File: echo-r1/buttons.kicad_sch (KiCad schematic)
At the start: 14 parts, among them SW1 DPAD↑, SW10 X, SW11 Y, SW12 START, SW13 SELECT, SW14 HOLD, SW2 DPAD↓, SW3 DPAD←, SW4 DPAD→, SW5 A, SW6 B, SW7 VOL+, SW8 VOL-, SW9 POWER

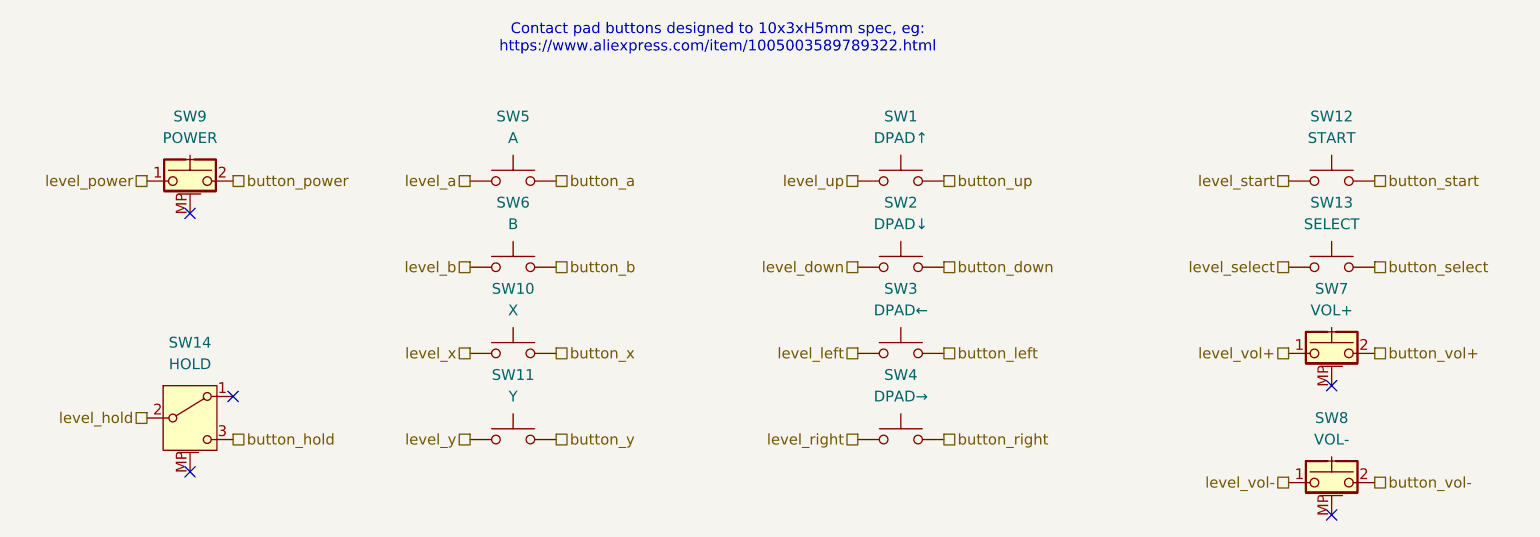
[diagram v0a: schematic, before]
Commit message: WIP redesign with STM32H7R3Z8J6
The H7R3 has a bunch of features that greatly simplify the design:
support for HyperRAM, which requires far fewer pins than SDRAM and
is more power efficient; this frees up the FMC to interface with the
display in 8-bit 8080 MCU mode; and there is a built-in USB HS PHY,
removing the need for an external PHY.

The huge reduction in signal count allows for a smaller pin count
package -- only 144 pins. HyperRAM only comes in BGA packages so it
makes sense to also use the UFBGA-144 package for the CPU, which
takes up less than 1/4 of the board area of an LQFP-176 package.
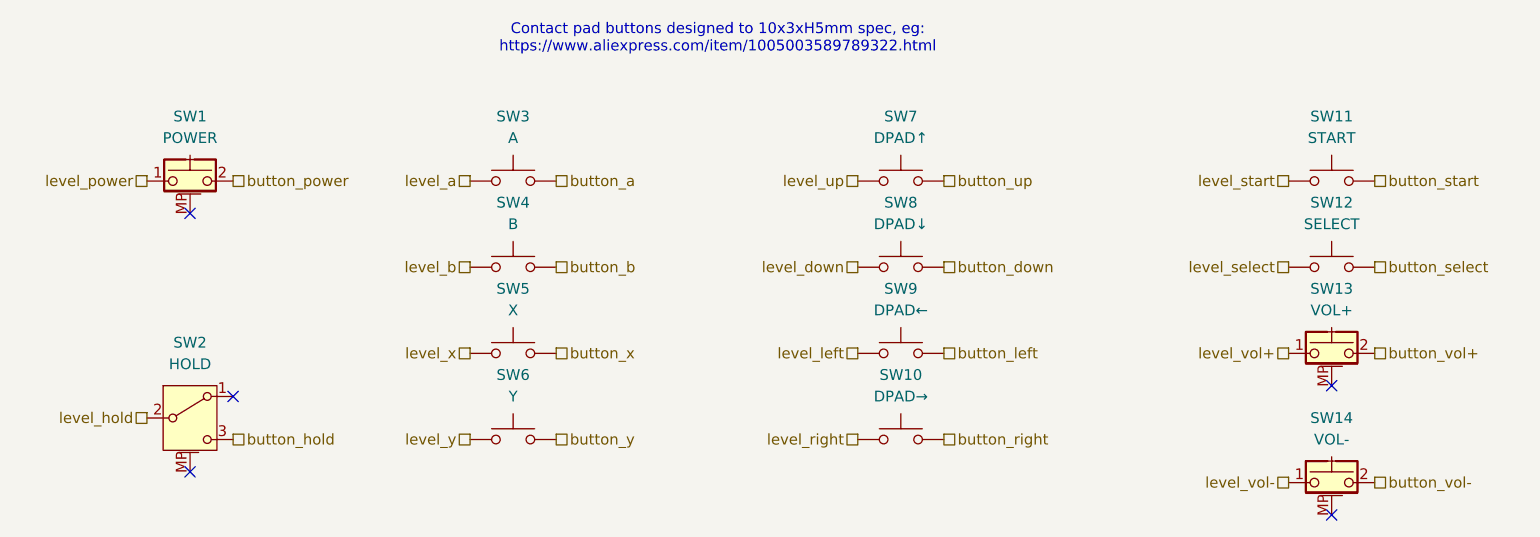
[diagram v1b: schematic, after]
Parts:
- renumbered SW9 to SW1, SW4 to SW10, SW12 to SW11, SW13 to SW12, SW7 to SW13, SW8 to SW14, SW14 to SW2, SW5 to SW3, SW6 to SW4, SW10 to SW5, SW11 to SW6, SW1 to SW7, SW2 to SW8, SW3 to SW9
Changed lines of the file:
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@@
 		(dnp no)
 		(fields_autoplaced yes)
-		(property "Reference" "SW6"
+		(property "Reference" "SW4"
 			(at 114.3 88.9 0)
 			(effects
@@
 			(project "echo-r1"
 				(path "/aa241847-30f4-429d-a148-6a6e39ba98e0/6b02ec5e-a793-4374-8df4-66bff795e3fc"
-					(reference "SW6")
+					(reference "SW4")
 					(unit 1)
 				)
@@
 		(dnp no)
 		(fields_autoplaced yes)
-		(property "Reference" "SW13"
+		(property "Reference" "SW12"
 			(at 210.82 88.9 0)
 			(effects
@@
 			(project "echo-r1"
 				(path "/aa241847-30f4-429d-a148-6a6e39ba98e0/6b02ec5e-a793-4374-8df4-66bff795e3fc"
-					(reference "SW13")
+					(reference "SW12")
 					(unit 1)
 				)
@@
 		(dnp no)
 		(fields_autoplaced yes)
-		(property "Reference" "SW1"
+		(property "Reference" "SW7"
 			(at 160.02 78.74 0)
 			(effects
@@
 			(project ""
 				(path "/aa241847-30f4-429d-a148-6a6e39ba98e0/6b02ec5e-a793-4374-8df4-66bff795e3fc"
-					(reference "SW1")
+					(reference "SW7")
 					(unit 1)
 				)
@@
 		(dnp no)
 		(fields_autoplaced yes)
-		(property "Reference" "SW10"
+		(property "Reference" "SW5"
 			(at 114.3 99.06 0)
 			(effects
@@
 			(project "echo-r1"
 				(path "/aa241847-30f4-429d-a148-6a6e39ba98e0/6b02ec5e-a793-4374-8df4-66bff795e3fc"
-					(reference "SW10")
+					(reference "SW5")
 					(unit 1)
 				)
@@
 		(dnp no)
 		(fields_autoplaced yes)
-		(property "Reference" "SW7"
+		(property "Reference" "SW13"
 			(at 210.82 99.06 0)
 			(effects
@@
 			(project "echo-r1"
 				(path "/aa241847-30f4-429d-a148-6a6e39ba98e0/6b02ec5e-a793-4374-8df4-66bff795e3fc"
-					(reference "SW7")
+					(reference "SW13")
 					(unit 1)
 				)
@@
 		(dnp no)
 		(fields_autoplaced yes)
-		(property "Reference" "SW14"
+		(property "Reference" "SW2"
 			(at 76.2 105.41 0)
 			(effects
@@
 			(project ""
 				(path "/aa241847-30f4-429d-a148-6a6e39ba98e0/6b02ec5e-a793-4374-8df4-66bff795e3fc"
-					(reference "SW14")
+					(reference "SW2")
 					(unit 1)
 				)
@@
 		(dnp no)
 		(fields_autoplaced yes)
-		(property "Reference" "SW9"
+		(property "Reference" "SW1"
 			(at 76.2 78.74 0)
 			(effects
@@
 			(project "echo-r1"
 				(path "/aa241847-30f4-429d-a148-6a6e39ba98e0/6b02ec5e-a793-4374-8df4-66bff795e3fc"
-					(reference "SW9")
+					(reference "SW1")
 					(unit 1)
 				)
@@
 		(dnp no)
 		(fields_autoplaced yes)
-		(property "Reference" "SW12"
+		(property "Reference" "SW11"
 			(at 210.82 78.74 0)
 			(effects
@@
 			(project "echo-r1"
 				(path "/aa241847-30f4-429d-a148-6a6e39ba98e0/6b02ec5e-a793-4374-8df4-66bff795e3fc"
-					(reference "SW12")
+					(reference "SW11")
 					(unit 1)
 				)
@@
 		(dnp no)
 		(fields_autoplaced yes)
-		(property "Reference" "SW8"
+		(property "Reference" "SW14"
 			(at 210.82 114.3 0)
 			(effects
@@
 			(project "echo-r1"
 				(path "/aa241847-30f4-429d-a148-6a6e39ba98e0/6b02ec5e-a793-4374-8df4-66bff795e3fc"
-					(reference "SW8")
+					(reference "SW14")
 					(unit 1)
 				)
@@
 		(dnp no)
 		(fields_autoplaced yes)
-		(property "Reference" "SW4"
+		(property "Reference" "SW10"
 			(at 160.02 109.22 0)
 			(effects
@@
 			(project "echo-r1"
 				(path "/aa241847-30f4-429d-a148-6a6e39ba98e0/6b02ec5e-a793-4374-8df4-66bff795e3fc"
-					(reference "SW4")
+					(reference "SW10")
 					(unit 1)
 				)
@@
 		(dnp no)
 		(fields_autoplaced yes)
-		(property "Reference" "SW11"
+		(property "Reference" "SW6"
 			(at 114.3 109.22 0)
 			(effects
@@
 			(project "echo-r1"
 				(path "/aa241847-30f4-429d-a148-6a6e39ba98e0/6b02ec5e-a793-4374-8df4-66bff795e3fc"
-					(reference "SW11")
+					(reference "SW6")
 					(unit 1)
 				)
@@
 		(dnp no)
 		(fields_autoplaced yes)
-		(property "Reference" "SW3"
+		(property "Reference" "SW9"
 			(at 160.02 99.06 0)
 			(effects
@@
 			(project "echo-r1"
 				(path "/aa241847-30f4-429d-a148-6a6e39ba98e0/6b02ec5e-a793-4374-8df4-66bff795e3fc"
-					(reference "SW3")
+					(reference "SW9")
 					(unit 1)
 				)
@@
 		(dnp no)
 		(fields_autoplaced yes)
-		(property "Reference" "SW5"
+		(property "Reference" "SW3"
 			(at 114.3 78.74 0)
 			(effects
@@
 			(project "echo-r1"
 				(path "/aa241847-30f4-429d-a148-6a6e39ba98e0/6b02ec5e-a793-4374-8df4-66bff795e3fc"
-					(reference "SW5")
+					(reference "SW3")
 					(unit 1)
 				)
@@
 		(dnp no)
 		(fields_autoplaced yes)
-		(property "Reference" "SW2"
+		(property "Reference" "SW8"
 			(at 160.02 88.9 0)
 			(effects
@@
 			(project "echo-r1"
 				(path "/aa241847-30f4-429d-a148-6a6e39ba98e0/6b02ec5e-a793-4374-8df4-66bff795e3fc"
-					(reference "SW2")
-					(unit 1)
-				)
+					(reference "SW8")
+					(unit 1)
+				)
